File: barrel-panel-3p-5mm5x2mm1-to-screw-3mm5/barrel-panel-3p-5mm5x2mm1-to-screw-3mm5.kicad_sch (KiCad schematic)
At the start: 1 part, among them J1 Barrel_Jack_Switch

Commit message: initial 3pin barrel connector footprint
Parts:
- J1: footprint (none) -> Connector_Barreljack_panel.pretty:BarrelJack_panel_3p_5.5mmx2.1mm_2_pins
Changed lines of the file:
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@@
     (property "Reference" "J1" (id 0) (at 132.08 78.74 0))
     (property "Value" "Barrel_Jack_Switch" (id 1) (at 132.08 81.28 0))
-    (property "Footprint" "" (id 2) (at 133.35 88.646 0)
+    (property "Footprint" "Connector_Barreljack_panel.pretty:BarrelJack_panel_3p_5.5mmx2.1mm_2_pins" (id 2) (at 133.35 88.646 0)
       (effects (font (size 1.27 1.27)) hide)
     )
@@
   (symbol_instances
     (path "/10764b11-b4da-492c-90ac-ab002632f8a8"
-      (reference "J1") (unit 1) (value "Barrel_Jack_Switch") (footprint "")
+      (reference "J1") (unit 1) (value "Barrel_Jack_Switch") (footprint "Connector_Barreljack_panel.pretty:BarrelJack_panel_3p_5.5mmx2.1mm_2_pins")
     )
   )

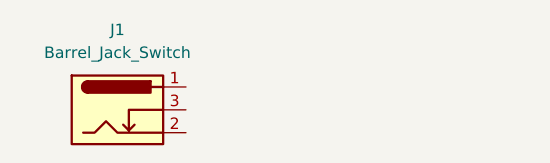
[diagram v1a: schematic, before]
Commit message: footprint finished, all elements placed in board
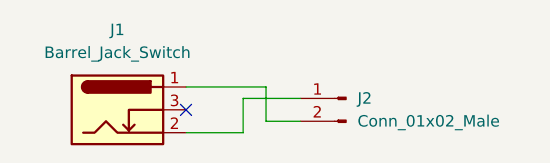
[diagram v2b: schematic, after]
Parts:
- added J2: Conn_01x02_Male, TerminalBlock_4Ucon:TerminalBlock_4Ucon_1x02_P3.50mm_Horizontal, symbol Connector:Conn_01x02_Male
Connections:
- net at J1.1: now also J2.2 (Pin_2)
- net at J1.2: now also J2.1 (Pin_1)
- no-connect marks 0 -> 1
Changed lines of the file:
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@@
 (kicad_sch (version 20211123) (generator eeschema)
   (paper "A4")
+  (no_connect (at 139.7 87.63))
+  (wire (pts (xy 152.4 88.9) (xy 148.59 88.9))
+    (stroke (width 0) (type default) (color 0 0 0 0))
+  )
+  (wire (pts (xy 146.05 86.36) (xy 152.4 86.36))
+    (stroke (width 0) (type default) (color 0 0 0 0))
+  )
+  (wire (pts (xy 148.59 88.9) (xy 148.59 85.09))
+    (stroke (width 0) (type default) (color 0 0 0 0))
+  )
+  (wire (pts (xy 139.7 85.09) (xy 148.59 85.09))
+    (stroke (width 0) (type default) (color 0 0 0 0))
+  )
+  (wire (pts (xy 146.05 86.36) (xy 146.05 90.17))
+    (stroke (width 0) (type default) (color 0 0 0 0))
+  )
+  (wire (pts (xy 139.7 90.17) (xy 146.05 90.17))
+    (stroke (width 0) (type default) (color 0 0 0 0))
+  )
   (symbol (lib_id "Connector:Barrel_Jack_Switch") (at 132.08 87.63 0) (unit 1)
     (in_bom yes) (on_board yes) (fields_autoplaced)
@@
     (pin "3")
   )
+  (symbol (lib_id "Connector:Conn_01x02_Male") (at 157.48 86.36 0) (mirror y) (unit 1)
+    (in_bom yes) (on_board yes) (fields_autoplaced)
+    (property "Reference" "J2" (id 0) (at 158.75 86.3599 0)
+      (effects (font (size 1.27 1.27)) (justify right))
+    )
+    (property "Value" "Conn_01x02_Male" (id 1) (at 158.75 88.8999 0)
+      (effects (font (size 1.27 1.27)) (justify right))
+    )
+    (property "Footprint" "TerminalBlock_4Ucon:TerminalBlock_4Ucon_1x02_P3.50mm_Horizontal" (id 2) (at 157.48 86.36 0)
+      (effects (font (size 1.27 1.27)) hide)
+    )
+    (property "Datasheet" "~" (id 3) (at 157.48 86.36 0)
+      (effects (font (size 1.27 1.27)) hide)
+    )
+    (pin "1")
+    (pin "2")
+  )
   (sheet_instances
     (path "/" (page "1"))
@@
       (reference "J1") (unit 1) (value "Barrel_Jack_Switch") (footprint "Connector_Barreljack_panel.pretty:BarrelJack_panel_3p_5.5mmx2.1mm_2_pins")
     )
+    (path "/c9233ca4-c5f7-42d1-8063-7d53b62d01dd"
+      (reference "J2") (unit 1) (value "Conn_01x02_Male") (footprint "TerminalBlock_4Ucon:TerminalBlock_4Ucon_1x02_P3.50mm_Horizontal")
+    )
   )

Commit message: single board gerbers
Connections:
- net at J1.1: now also J2.1 (Pin_1); no longer J2.2 (Pin_2)
- net at J1.2: now also J2.2 (Pin_2); no longer J2.1 (Pin_1)
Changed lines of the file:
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@@
   (paper "A4")
   (no_connect (at 139.7 87.63))
-  (wire (pts (xy 152.4 88.9) (xy 148.59 88.9))
+  (wire (pts (xy 146.05 85.09) (xy 146.05 86.36))
+    (stroke (width 0) (type default) (color 0 0 0 0))
+  )
+  (wire (pts (xy 139.7 90.17) (xy 146.05 90.17))
     (stroke (width 0) (type default) (color 0 0 0 0))
   )
@@
     (stroke (width 0) (type default) (color 0 0 0 0))
   )
-  (wire (pts (xy 148.59 88.9) (xy 148.59 85.09))
+  (wire (pts (xy 146.05 90.17) (xy 146.05 88.9))
     (stroke (width 0) (type default) (color 0 0 0 0))
   )
-  (wire (pts (xy 139.7 85.09) (xy 148.59 85.09))
+  (wire (pts (xy 139.7 85.09) (xy 146.05 85.09))
     (stroke (width 0) (type default) (color 0 0 0 0))
   )
-  (wire (pts (xy 146.05 86.36) (xy 146.05 90.17))
+  (wire (pts (xy 146.05 88.9) (xy 152.4 88.9))
     (stroke (width 0) (type default) (color 0 0 0 0))
   )
-  (wire (pts (xy 139.7 90.17) (xy 146.05 90.17))
-    (stroke (width 0) (type default) (color 0 0 0 0))
-  )

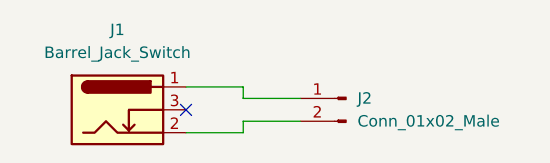
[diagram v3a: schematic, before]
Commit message: fixed board to ease nut insertion
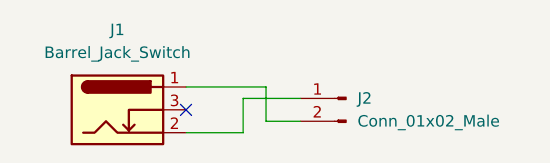
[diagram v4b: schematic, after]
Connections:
- net at J1.1: now also J2.2 (Pin_2); no longer J2.1 (Pin_1)
- net at J1.2: now also J2.1 (Pin_1); no longer J2.2 (Pin_2)
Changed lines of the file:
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@@
   (paper "A4")
   (no_connect (at 139.7 87.63))
-  (wire (pts (xy 146.05 85.09) (xy 146.05 86.36))
+  (wire (pts (xy 139.7 90.17) (xy 146.05 90.17))
     (stroke (width 0) (type default) (color 0 0 0 0))
   )
-  (wire (pts (xy 139.7 90.17) (xy 146.05 90.17))
+  (wire (pts (xy 148.59 85.09) (xy 148.59 88.9))
+    (stroke (width 0) (type default) (color 0 0 0 0))
+  )
+  (wire (pts (xy 148.59 88.9) (xy 152.4 88.9))
+    (stroke (width 0) (type default) (color 0 0 0 0))
+  )
+  (wire (pts (xy 146.05 86.36) (xy 146.05 90.17))
     (stroke (width 0) (type default) (color 0 0 0 0))
   )
@@
     (stroke (width 0) (type default) (color 0 0 0 0))
   )
-  (wire (pts (xy 146.05 90.17) (xy 146.05 88.9))
+  (wire (pts (xy 139.7 85.09) (xy 148.59 85.09))
     (stroke (width 0) (type default) (color 0 0 0 0))
   )
-  (wire (pts (xy 139.7 85.09) (xy 146.05 85.09))
-    (stroke (width 0) (type default) (color 0 0 0 0))
-  )
-  (wire (pts (xy 146.05 88.9) (xy 152.4 88.9))
-    (stroke (width 0) (type default) (color 0 0 0 0))
-  )
